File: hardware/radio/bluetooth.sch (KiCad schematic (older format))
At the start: 5 parts, among them U401 BLE113

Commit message: Assign testpoint footprints
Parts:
- C401, C402, C403: footprint (none) -> Capacitors_SMD:C_0603
- R401: footprint (none) -> Resistors_SMD:R_0603
- U401: footprint (none) -> footprints_:BLE113
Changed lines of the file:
@@
 F 0 "U401" H 4400 4200 60  0000 C CNN
 F 1 "BLE113" H 4400 4100 60  0000 C CNN
-F 2 "" H 4400 3300 60  0000 C CNN
+F 2 "footprints_:BLE113" H 4400 3300 60  0001 C CNN
 F 3 "" H 4400 3300 60  0000 C CNN
 	1    4400 3300
@@
 Connection ~ 3650 4900
 $Comp
-L GND #PWR040
+L GND #PWR041
 U 1 1 55EB72D9
 P 3650 5150
-F 0 "#PWR040" H 3650 4900 50  0001 C CNN
+F 0 "#PWR041" H 3650 4900 50  0001 C CNN
 F 1 "GND" H 3650 5000 50  0000 C CNN
 F 2 "" H 3650 5150 60  0000 C CNN
@@
 F 0 "C401" H 3525 3500 50  0000 L CNN
 F 1 "470n" H 3500 3250 50  0000 L CNN
-F 2 "" H 3538 3250 30  0000 C CNN
+F 2 "Capacitors_SMD:C_0603" H 3538 3250 30  0001 C CNN
 F 3 "" H 3500 3400 60  0000 C CNN
 	1    3500 3400
@@
 F 0 "C402" H 3725 3500 50  0000 L CNN
 F 1 "470n" H 3700 3250 50  0000 L CNN
-F 2 "" H 3738 3250 30  0000 C CNN
+F 2 "Capacitors_SMD:C_0603" H 3738 3250 30  0001 C CNN
 F 3 "" H 3700 3400 60  0000 C CNN
 	1    3700 3400
@@
 F 0 "C403" H 3925 3500 50  0000 L CNN
 F 1 "470n" H 3900 3250 50  0000 L CNN
-F 2 "" H 3938 3250 30  0000 C CNN
+F 2 "Capacitors_SMD:C_0603" H 3938 3250 30  0001 C CNN
 F 3 "" H 3900 3400 60  0000 C CNN
 	1    3900 3400
@@
 F 0 "R401" V 3080 2450 50  0000 C CNN
 F 1 "10k" V 3000 2450 50  0000 C CNN
-F 2 "" V 2930 2450 30  0000 C CNN
+F 2 "Resistors_SMD:R_0603" V 2930 2450 30  0001 C CNN
 F 3 "" H 3000 2450 30  0000 C CNN
 	1    3000 2450
@@
 Connection ~ 3550 2600
 $Comp
-L VCC #PWR041
+L VCC #PWR042
 U 1 1 55EB8217
 P 3550 2400
-F 0 "#PWR041" H 3550 2250 50  0001 C CNN
+F 0 "#PWR042" H 3550 2250 50  0001 C CNN
 F 1 "VCC" H 3550 2550 50  0000 C CNN
 F 2 "" H 3550 2400 60  0000 C CNN
@@
 $EndComp
 $Comp
-L VCC #PWR042
+L VCC #PWR043
 U 1 1 55EB8235
 P 3000 2150
-F 0 "#PWR042" H 3000 2000 50  0001 C CNN
+F 0 "#PWR043" H 3000 2000 50  0001 C CNN
 F 1 "VCC" H 3000 2300 50  0000 C CNN
 F 2 "" H 3000 2150 60  0000 C CNN

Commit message: Work on laying out TPs
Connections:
- net VCC renamed VCC_BLE
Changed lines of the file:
@@
 P2_2-PROG
 Text HLabel 9400 4500 2    60   Input ~ 0
-VCC
+VCC_BLE
 Text HLabel 9400 4600 2    60   Input ~ 0
 GND
@@
 Wire Bus Line
 	3400 2200 5650 2200
-Text Label 3800 2600 2    60   ~ 0
-VCC
+Text Label 3550 2400 0    60   ~ 0
+VCC_BLE
 Text Label 3850 4000 2    60   ~ 0
 GND
@@
 Connection ~ 3650 4900
 $Comp
-L GND #PWR041
+L GND #PWR038
 U 1 1 55EB72D9
 P 3650 5150
-F 0 "#PWR041" H 3650 4900 50  0001 C CNN
+F 0 "#PWR038" H 3650 4900 50  0001 C CNN
 F 1 "GND" H 3650 5000 50  0000 C CNN
 F 2 "" H 3650 5150 60  0000 C CNN
@@
 GND
 Text Label 9350 4500 2    60   ~ 0
-VCC
+VCC_BLE
 Text Label 9350 4400 2    60   ~ 0
 P2_2-PROG
@@
 	3550 2600 3550 2400
 Connection ~ 3550 2600
-$Comp
-L VCC #PWR042
-U 1 1 55EB8217
-P 3550 2400
-F 0 "#PWR042" H 3550 2250 50  0001 C CNN
-F 1 "VCC" H 3550 2550 50  0000 C CNN
-F 2 "" H 3550 2400 60  0000 C CNN
-F 3 "" H 3550 2400 60  0000 C CNN
-	1    3550 2400
-	1    0    0    -1
-$EndComp
-$Comp
-L VCC #PWR043
-U 1 1 55EB8235
-P 3000 2150
-F 0 "#PWR043" H 3000 2000 50  0001 C CNN
-F 1 "VCC" H 3000 2300 50  0000 C CNN
-F 2 "" H 3000 2150 60  0000 C CNN
-F 3 "" H 3000 2150 60  0000 C CNN
-	1    3000 2150
-	1    0    0    -1
-$EndComp
 Wire Wire Line
 	3000 2150 3000 2300
+Text Label 3000 2150 0    60   ~ 0
+VCC_BLE
 $EndSCHEMATC

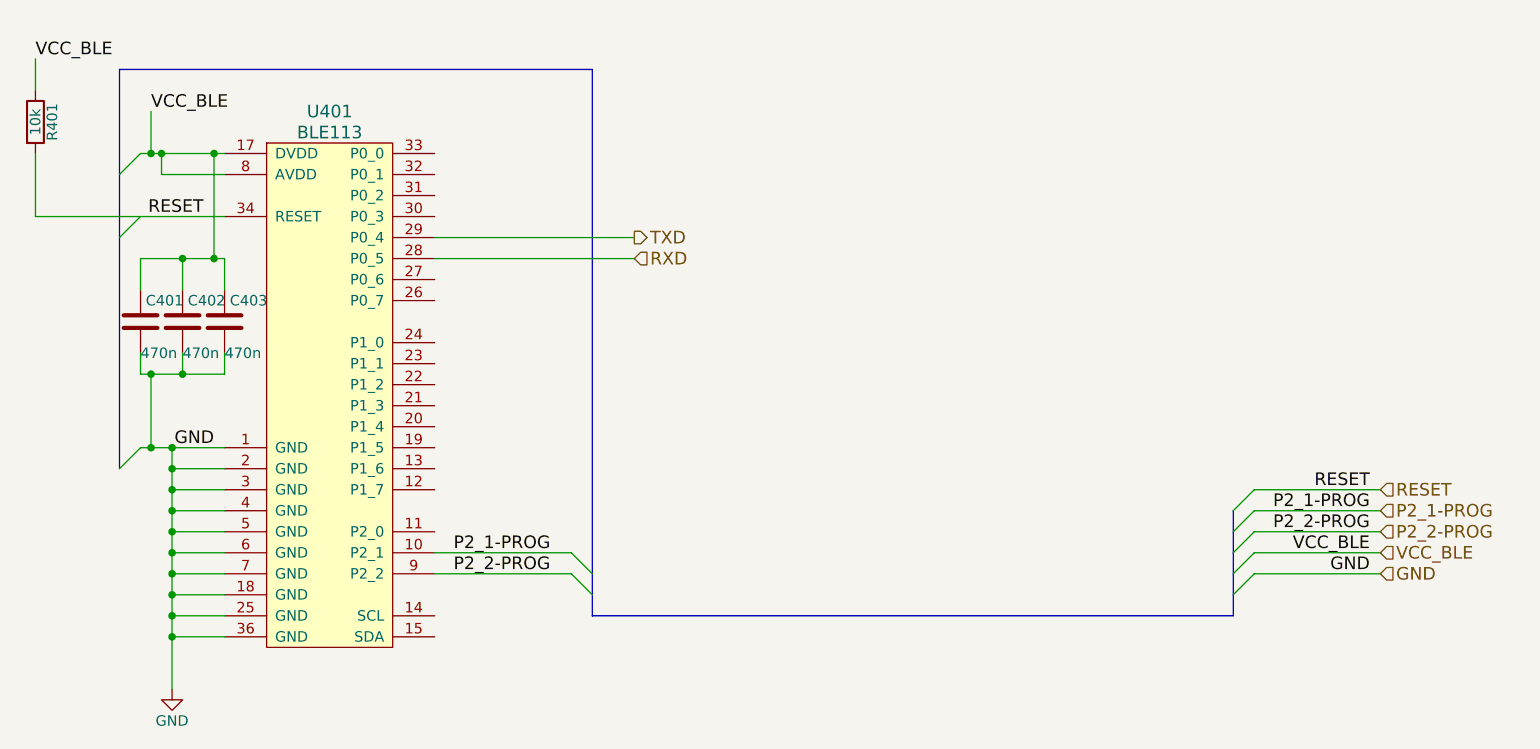
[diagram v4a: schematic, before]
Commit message: compress schematic for embedding images in thesis
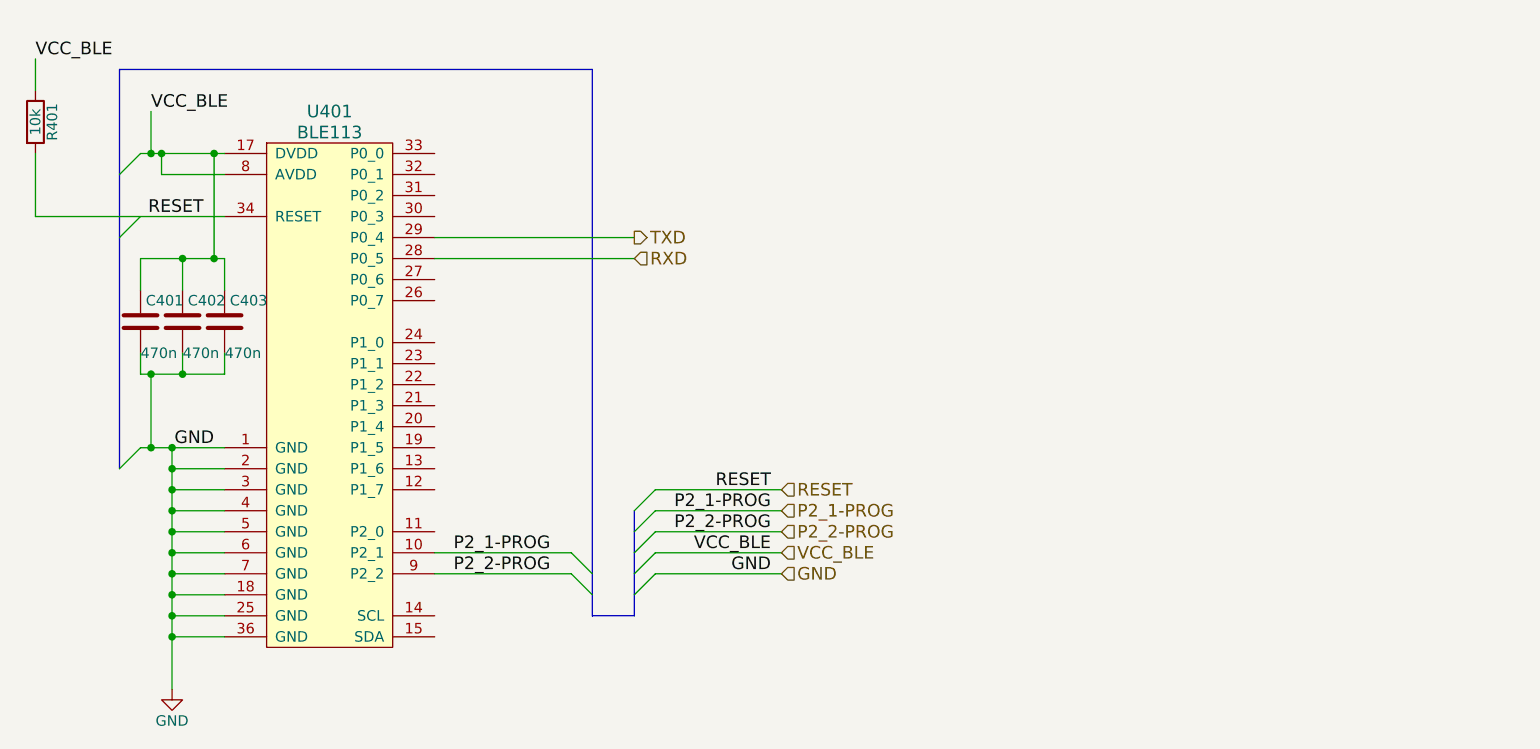
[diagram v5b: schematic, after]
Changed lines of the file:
@@
 	5550 4600 5650 4700
 Wire Bus Line
-	5650 2200 5650 4800
-Wire Bus Line
-	5650 4800 8700 4800
-Wire Bus Line
-	8700 4800 8700 4300
+	5650 2200 5650 4600
+Wire Bus Line
+	5650 4600 5650 4700
+Wire Bus Line
+	5650 4700 5650 4800
+Wire Bus Line
+	5650 4800 5850 4800
+Wire Bus Line
+	5850 4800 5850 4700
+Wire Bus Line
+	5850 4700 5850 4600
+Wire Bus Line
+	5850 4600 5850 4500
+Wire Bus Line
+	5850 4500 5850 4400
+Wire Bus Line
+	5850 4400 5850 4300
 Text Label 3800 2900 2    60   ~ 0
 RESET
@@
 P2_1-PROG
 Entry Wire Line
-	8700 4700 8800 4600
-Entry Wire Line
-	8700 4600 8800 4500
-Entry Wire Line
-	8700 4500 8800 4400
-Entry Wire Line
-	8700 4400 8800 4300
-Entry Wire Line
-	8700 4300 8800 4200
-Wire Wire Line
-	8800 4200 9400 4200
-Wire Wire Line
-	8800 4300 9400 4300
-Wire Wire Line
-	8800 4400 9400 4400
-Wire Wire Line
-	8800 4500 9400 4500
-Wire Wire Line
-	8800 4600 9400 4600
-Text HLabel 9400 4200 2    60   Input ~ 0
+	5850 4700 5950 4600
+Entry Wire Line
+	5850 4600 5950 4500
+Entry Wire Line
+	5850 4500 5950 4400
+Entry Wire Line
+	5850 4400 5950 4300
+Entry Wire Line
+	5850 4300 5950 4200
+Wire Wire Line
+	5950 4200 6550 4200
+Wire Wire Line
+	5950 4300 6550 4300
+Wire Wire Line
+	5950 4400 6550 4400
+Wire Wire Line
+	5950 4500 6550 4500
+Wire Wire Line
+	5950 4600 6550 4600
+Text HLabel 6550 4200 2    60   Input ~ 0
 RESET
-Text HLabel 9400 4300 2    60   Input ~ 0
+Text HLabel 6550 4300 2    60   Input ~ 0
 P2_1-PROG
-Text HLabel 9400 4400 2    60   Input ~ 0
+Text HLabel 6550 4400 2    60   Input ~ 0
 P2_2-PROG
-Text HLabel 9400 4500 2    60   Input ~ 0
+Text HLabel 6550 4500 2    60   Input ~ 0
 VCC_BLE
-Text HLabel 9400 4600 2    60   Input ~ 0
+Text HLabel 6550 4600 2    60   Input ~ 0
 GND
 Entry Wire Line
 	3400 3000 3500 2900
 Wire Wire Line
-	3500 4000 3900 4000
+	3500 4000 3550 4000
+Wire Wire Line
+	3550 4000 3650 4000
+Wire Wire Line
+	3650 4000 3900 4000
 Entry Wire Line
 	3400 4100 3500 4000
@@
 	3400 2700 3500 2600
 Wire Wire Line
-	3900 2600 3500 2600
-Wire Bus Line
-	3400 2200 3400 4100
+	3900 2600 3850 2600
+Wire Wire Line
+	3850 2600 3600 2600
+Wire Wire Line
+	3600 2600 3550 2600
+Wire Wire Line
+	3550 2600 3500 2600
+Wire Bus Line
+	3400 2200 3400 2700
+Wire Bus Line
+	3400 2700 3400 3000
+Wire Bus Line
+	3400 3000 3400 4100
 Wire Bus Line
 	3400 2200 5650 2200
@@
 	3900 4100 3650 4100
 Wire Wire Line
-	3650 4000 3650 5150
+	3650 4000 3650 4100
+Wire Wire Line
+	3650 4100 3650 4200
+Wire Wire Line
+	3650 4200 3650 4300
+Wire Wire Line
+	3650 4300 3650 4400
+Wire Wire Line
+	3650 4400 3650 4500
+Wire Wire Line
+	3650 4500 3650 4600
+Wire Wire Line
+	3650 4600 3650 4700
+Wire Wire Line
+	3650 4700 3650 4800
+Wire Wire Line
+	3650 4800 3650 4900
+Wire Wire Line
+	3650 4900 3650 5150
 Connection ~ 3650 4000
 Connection ~ 3650 4100
@@
 	1    0    0    -1
 $EndComp
-Text Label 9350 4600 2    60   ~ 0
+Text Label 6500 4600 2    60   ~ 0
 GND
-Text Label 9350 4500 2    60   ~ 0
+Text Label 6500 4500 2    60   ~ 0
 VCC_BLE
-Text Label 9350 4400 2    60   ~ 0
+Text Label 6500 4400 2    60   ~ 0
 P2_2-PROG
-Text Label 9350 4300 2    60   ~ 0
+Text Label 6500 4300 2    60   ~ 0
 P2_1-PROG
-Text Label 9350 4200 2    60   ~ 0
+Text Label 6500 4200 2    60   ~ 0
 RESET
 Wire Wire Line
@@
 	3850 2600 3850 3100
 Wire Wire Line
-	3500 3100 3900 3100
+	3500 3100 3700 3100
+Wire Wire Line
+	3700 3100 3850 3100
+Wire Wire Line
+	3850 3100 3900 3100
 Wire Wire Line
 	3900 3100 3900 3250
@@
 	3500 3550 3500 3650
 Wire Wire Line
-	3500 3650 3900 3650
+	3500 3650 3550 3650
+Wire Wire Line
+	3550 3650 3700 3650
+Wire Wire Line
+	3700 3650 3900 3650
 Wire Wire Line
 	3900 3650 3900 3550

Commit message: Compress schematics for screenshots
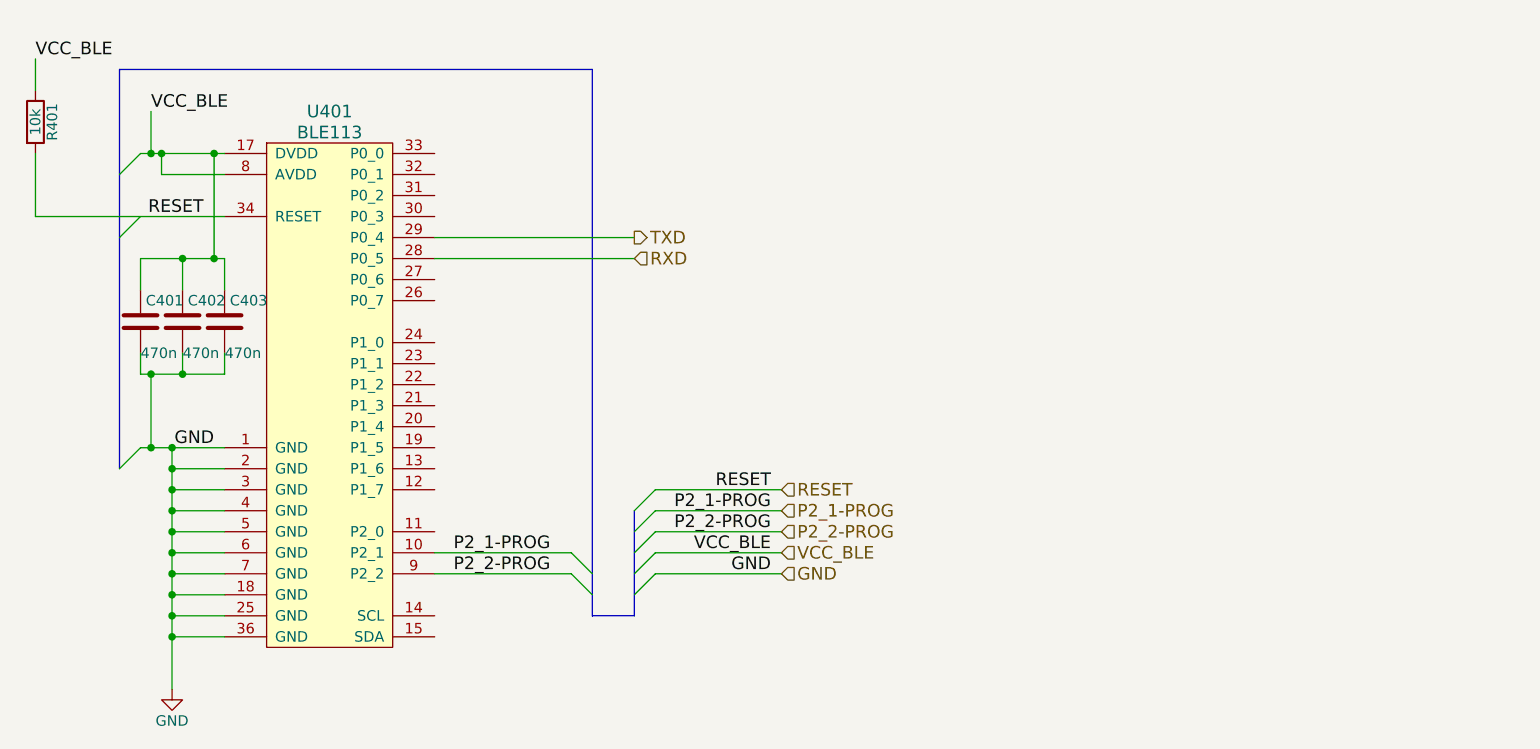
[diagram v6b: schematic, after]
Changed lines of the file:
@@
 	5550 4600 5650 4700
 Wire Bus Line
-	5650 2200 5650 4600
+	5650 2200 5650 4800
 Wire Bus Line
-	5650 4600 5650 4700
+	5850 4800 5650 4800
 Wire Bus Line
-	5650 4700 5650 4800
-Wire Bus Line
-	5650 4800 5850 4800
-Wire Bus Line
-	5850 4800 5850 4700
-Wire Bus Line
-	5850 4700 5850 4600
-Wire Bus Line
-	5850 4600 5850 4500
-Wire Bus Line
-	5850 4500 5850 4400
-Wire Bus Line
-	5850 4400 5850 4300
+	5850 4300 5850 4800
 Text Label 3800 2900 2    60   ~ 0
 RESET
@@
 	3400 3000 3500 2900
 Wire Wire Line
-	3500 4000 3550 4000
-Wire Wire Line
-	3550 4000 3650 4000
-Wire Wire Line
-	3650 4000 3900 4000
+	3500 4000 3900 4000
 Entry Wire Line
 	3400 4100 3500 4000
@@
 	3400 2700 3500 2600
 Wire Wire Line
-	3900 2600 3850 2600
-Wire Wire Line
-	3850 2600 3600 2600
-Wire Wire Line
-	3600 2600 3550 2600
-Wire Wire Line
-	3550 2600 3500 2600
+	3500 2600 3900 2600
 Wire Bus Line
-	3400 2200 3400 2700
-Wire Bus Line
-	3400 2700 3400 3000
-Wire Bus Line
-	3400 3000 3400 4100
+	3400 2200 3400 4100
 Wire Bus Line
 	3400 2200 5650 2200
@@
 	3900 4100 3650 4100
 Wire Wire Line
-	3650 4000 3650 4100
-Wire Wire Line
-	3650 4100 3650 4200
-Wire Wire Line
-	3650 4200 3650 4300
-Wire Wire Line
-	3650 4300 3650 4400
-Wire Wire Line
-	3650 4400 3650 4500
-Wire Wire Line
-	3650 4500 3650 4600
-Wire Wire Line
-	3650 4600 3650 4700
-Wire Wire Line
-	3650 4700 3650 4800
-Wire Wire Line
-	3650 4800 3650 4900
-Wire Wire Line
-	3650 4900 3650 5150
+	3650 4000 3650 5150
 Connection ~ 3650 4000
 Connection ~ 3650 4100
@@
 $EndComp
 Wire Wire Line
-	3850 2600 3850 3100
+	3850 3100 3850 2600
 Wire Wire Line
-	3500 3100 3700 3100
-Wire Wire Line
-	3700 3100 3850 3100
-Wire Wire Line
-	3850 3100 3900 3100
+	3500 3100 3900 3100
 Wire Wire Line
 	3900 3100 3900 3250
@@
 	3500 3550 3500 3650
 Wire Wire Line
-	3500 3650 3550 3650
-Wire Wire Line
-	3550 3650 3700 3650
-Wire Wire Line
-	3700 3650 3900 3650
+	3500 3650 3900 3650
 Wire Wire Line
 	3900 3650 3900 3550
